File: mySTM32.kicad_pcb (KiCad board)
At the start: 2 copper layers, 138 x 108 mm, 122 parts, among them J1 conn1X2, J10 DB9_Female****, J11 USB_OTG, J12 conn2X16, J13 conn2X3, J14 Conn_02x02, J15 conn2X3, J16 conn1X2, J17 conn2X2, J18 JTAG, J19 Conn_02x17_Odd_Even, J2 USB_OTG, J20 Conn_02x22_Odd_Even, J21 conn2X9, J22 conn2X3, J23 Conn2x4, J3 conn2X3, J4 conn2X2, J5 conn2X2, J6 conn1X2, J7 Conn_01x02, J8 Conn2x4, J9 conn2X4, Q1 Q_NPN_BEC(S8050), Q2 Q_NPN_BEC, Q3 Q_NPN_BEC(S8050), SW1 KFT8.0, SW2 WAKUP, SW3 RESET, SW4 KE1, SW5 KEY2, U1 AT24C02, U2 W25Q16, U3 SD-Card, U4 SP3485, U5 SN65HVD230, U6 CH340G, U7 AMS1117, U8 SP3232, U9 STM32F103VET6, Y1 12MHz, Y2 32.768KHz, Y3 8MHz

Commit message: [IR Tx] [IR Rx]
Signed-off-by: EasonLiang <liangyx25@163.com>
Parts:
- moved R4 0.58 mm to (48.9, 117.2)
- moved R2 0.40 mm to (46.0, 117.1)
- moved R1 0.31 mm to (42.6, 117.1)
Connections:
- J5 pad 1: /IE -> /IR
- J5 pad 2: /PB1 -> /PB0
- J5 pad 3: /IR -> /IE
- J5 pad 4: /PB0 -> /PB1
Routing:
- net +3V3: track 140.4 -> 167.4 mm
- net /PB1: track 31.7 -> 53.5 mm
- net /PB0: track 34.0 -> 55.8 mm
- net Net-(D1-Pad1): track 0.00 -> 11.3 mm
- net Net-(D1-Pad2): track 0.00 -> 9.07 mm
- net /IR: track 0.00 -> 9.05 mm
- net Net-(Q1-Pad1): track 0.00 -> 8.27 mm
- net /IE: track 0.00 -> 8.22 mm
- net GND: track 89.5 -> 92.9 mm
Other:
- board text added: "PB0"
- board text added: "PB1"
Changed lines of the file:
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@@
   (general
     (thickness 1.6)
-    (drawings 99)
-    (tracks 556)
+    (drawings 101)
+    (tracks 587)
     (zones 0)
     (modules 122)
@@
   )
   (module Resistor_SMD:R_0805_2012Metric (layer F.Cu)
-    (at 48.91532 116.62156 270)
+    (at 48.87214 117.19814 270)
     (descr "Resistor SMD 0805 (2012 Metric), square (rectangular) end terminal, IPC_7351 nominal, (Body size source: IPC-SM-782 page 72, https://www.pcb-3d.com/wordpress/wp-content/uploads/ipc-sm-782a_amendment_1_and_2.pdf), generated with kicad-footprint-generator")
     (tags resistor)
@@
   )
   (module Resistor_SMD:R_0603_1608Metric (layer F.Cu)
-    (at 45.74032 116.82156 270)
+    (at 45.99686 117.12448 270)
     (descr "Resistor SMD 0603 (1608 Metric), square (rectangular) end terminal, IPC_7351 nominal, (Body size source: IPC-SM-782 page 72, https://www.pcb-3d.com/wordpress/wp-content/uploads/ipc-sm-782a_amendment_1_and_2.pdf), generated with kicad-footprint-generator")
     (tags resistor)
@@
   )
   (module Resistor_SMD:R_0603_1608Metric (layer F.Cu)
-    (at 42.56532 116.82156 90)
+    (at 42.57548 117.13464 90)
     (descr "Resistor SMD 0603 (1608 Metric), square (rectangular) end terminal, IPC_7351 nominal, (Body size source: IPC-SM-782 page 72, https://www.pcb-3d.com/wordpress/wp-content/uploads/ipc-sm-782a_amendment_1_and_2.pdf), generated with kicad-footprint-generator")
     (tags resistor)
@@
     (fp_line (start -1.27 2.54) (end 3.81 2.54) (layer F.SilkS) (width 0.12))
     (pad 4 thru_hole circle (at 2.54 -1.27) (size 1.6 1.6) (drill 1.02) (layers *.Cu *.Mask)
-      (net 45 /PB0))
+      (net 46 /PB1))
     (pad 3 thru_hole circle (at 2.54 1.27) (size 1.6 1.6) (drill 1.02) (layers *.Cu *.Mask)
-      (net 22 /IR))
+      (net 47 /IE))
     (pad 2 thru_hole circle (at 0 -1.27) (size 1.6 1.6) (drill 1.02) (layers *.Cu *.Mask)
-      (net 46 /PB1))
+      (net 45 /PB0))
     (pad 1 thru_hole rect (at 0 1.27) (size 1.6 1.6) (drill 1.02) (layers *.Cu *.Mask)
-      (net 47 /IE))
+      (net 22 /IR))
     (model ${KISYS3DMOD}/Connector_PinHeader_2.54mm.3dshapes/PinHeader_2x02_P2.54mm_Vertical.wrl
       (offset (xyz 0 -1 0))
@@
     )
   )
+  (gr_text PB1 (at 45.76064 104.3813) (layer F.SilkS)
+    (effects (font (size 1.2 1) (thickness 0.25)))
+  )
+  (gr_text PB0 (at 42.61612 104.3813) (layer F.SilkS)
+    (effects (font (size 1.2 1) (thickness 0.25)))
+  )
   (gr_text PB10 (at 137.09142 118.22938) (layer F.SilkS)
     (effects (font (size 1.2 1) (thickness 0.25)))
@@
   (gr_line (start 50.6984 121.8) (end 61.849 121.8) (layer F.SilkS) (width 0.12))
   (gr_line (start 50.6984 114.6) (end 50.6984 138) (layer F.SilkS) (width 0.12))
-  (gr_line (start 58.65368 103.67766) (end 30.05328 103.67766) (layer F.SilkS) (width 0.12))
+  (gr_line (start 58.65368 103.4) (end 30.05328 103.4) (layer F.SilkS) (width 0.12))
   (gr_line (start 58.6994 121.8) (end 58.6994 72.009) (layer F.SilkS) (width 0.12))
   (gr_line (start 30.0482 88.19526) (end 58.6994 88.19526) (layer F.SilkS) (width 0.12))
@@
   (segment (start 152.94386 114.81136) (end 152.94386 111.93018) (width 0.254) (layer F.Cu) (net 1))
   (segment (start 159.5755 121.443) (end 152.94386 114.81136) (width 0.254) (layer F.Cu) (net 1))
+  (segment (start 38.49878 115.4041) (end 37.85032 116.05256) (width 0.508) (layer F.Cu) (net 1))
+  (segment (start 38.49878 112.91346) (end 38.49878 115.4041) (width 0.508) (layer F.Cu) (net 1))
   (segment (start 96.880062 90.385849) (end 96.847552 90.385849) (width 0.254) (layer F.Cu) (net 3))
   (segment (start 92.443 85.916275) (end 92.443 85.344) (width 0.254) (layer F.Cu) (net 3))
@@
   (segment (start 140.87632 120.0785) (end 140.6652 120.28962) (width 0.254) (layer F.Cu) (net 3))
   (segment (start 143.3325 120.0785) (end 140.87632 120.0785) (width 0.254) (layer F.Cu) (net 3))
+  (segment (start 50.02615 129.55355) (end 54.5465 134.0739) (width 0.508) (layer F.Cu) (net 3))
+  (segment (start 50.02615 117.43965) (end 50.02615 129.55355) (width 0.508) (layer F.Cu) (net 3))
+  (segment (start 48.87214 116.28564) (end 50.02615 117.43965) (width 0.508) (layer F.Cu) (net 3))
+  (segment (start 38.49848 111.36376) (end 38.49878 111.36346) (width 0.508) (layer F.Cu) (net 3))
+  (segment (start 35.01898 111.36376) (end 38.49848 111.36376) (width 0.508) (layer F.Cu) (net 3))
+  (segment (start 38.49878 107.94696) (end 38.49878 108.0389) (width 0.508) (layer F.Cu) (net 3))
+  (segment (start 38.49878 108.0389) (end 38.49878 111.36346) (width 0.508) (layer F.Cu) (net 3))
   (segment (start 153.4795 74.4985) (end 153.29438 74.68362) (width 0.254) (layer F.Cu) (net 4))
   (segment (start 153.4795 71.361) (end 153.4795 74.4985) (width 0.254) (layer F.Cu) (net 4))
@@
   (segment (start 90.217394 85.81199) (end 88.36901 85.81199) (width 0.254) (layer F.Cu) (net 19))
   (segment (start 87.567 86.614) (end 83.833 86.614) (width 0.254) (layer F.Cu) (net 19))
+  (segment (start 48.87214 120.52554) (end 44.16552 125.23216) (width 0.508) (layer F.Cu) (net 20))
+  (segment (start 48.87214 118.11064) (end 48.87214 120.52554) (width 0.508) (layer F.Cu) (net 20))
+  (segment (start 35.85032 117.00256) (end 35.85032 116.91798) (width 0.254) (layer F.Cu) (net 21))
+  (segment (start 40.63192 122.69216) (end 44.16552 122.69216) (width 0.508) (layer F.Cu) (net 21))
+  (segment (start 35.85032 117.91056) (end 40.63192 122.69216) (width 0.508) (layer F.Cu) (net 21))
+  (segment (start 35.85032 117.00256) (end 35.85032 117.91056) (width 0.508) (layer F.Cu) (net 21))
+  (segment (start 35.01898 106.28376) (end 35.01898 106.4514) (width 0.508) (layer F.Cu) (net 22))
+  (segment (start 35.01898 106.4514) (end 38.34434 106.4514) (width 0.508) (layer F.Cu) (net 22))
+  (segment (start 38.49878 106.29696) (end 38.34434 106.4514) (width 0.508) (layer F.Cu) (net 22))
+  (segment (start 39.70578 106.29696) (end 42.62628 109.21746) (width 0.508) (layer F.Cu) (net 22))
+  (segment (start 38.49878 106.29696) (end 39.70578 106.29696) (width 0.508) (layer F.Cu) (net 22))
   (segment (start 151.7165 60.706) (end 151.78 60.6425) (width 0.508) (layer F.Cu) (net 23))
   (segment (start 149.034 60.706) (end 151.7165 60.706) (width 0.508) (layer F.Cu) (net 23))
@@
   (segment (start 90.48568 105.512999) (end 64.627001 105.512999) (width 0.254) (layer F.Cu) (net 45))
   (segment (start 95.112295 100.886384) (end 90.48568 105.512999) (width 0.254) (layer F.Cu) (net 45))
+  (segment (start 62.410459 105.550459) (end 63.5 106.64) (width 0.254) (layer F.Cu) (net 45))
+  (segment (start 43.753281 105.550459) (end 62.410459 105.550459) (width 0.254) (layer F.Cu) (net 45))
+  (segment (start 42.62628 106.67746) (end 43.753281 105.550459) (width 0.254) (layer F.Cu) (net 45))
   (segment (start 90.065787 106.64) (end 66.04 106.64) (width 0.254) (layer F.Cu) (net 46))
   (segment (start 95.465849 101.239938) (end 90.065787 106.64) (width 0.254) (layer F.Cu) (net 46))
+  (segment (start 65.167962 106.64) (end 66.04 106.64) (width 0.254) (layer F.Cu) (net 46))
+  (segment (start 64.040961 107.767001) (end 65.167962 106.64) (width 0.254) (layer F.Cu) (net 46))
+  (segment (start 46.255821 107.767001) (end 64.040961 107.767001) (width 0.254) (layer F.Cu) (net 46))
+  (segment (start 45.16628 106.67746) (end 46.255821 107.767001) (width 0.254) (layer F.Cu) (net 46))
+  (segment (start 45.16628 109.21746) (end 45.16628 113.81486) (width 0.508) (layer F.Cu) (net 47))
+  (segment (start 42.6715 116.30964) (end 42.57548 116.30964) (width 0.508) (layer F.Cu) (net 47))
+  (segment (start 45.16628 113.81486) (end 42.6715 116.30964) (width 0.508) (layer F.Cu) (net 47))
   (segment (start 136.1148 36.53612) (end 132.98882 39.6621) (width 0.254) (layer F.Cu) (net 48))
   (segment (start 136.1148 34.1122) (end 136.1148 36.53612) (width 0.254) (layer F.Cu) (net 48))
@@
   (segment (start 126.463145 66) (end 129.54 66) (width 0.254) (layer F.Cu) (net 149))
   (segment (start 104.198617 88.264528) (end 126.463145 66) (width 0.254) (layer F.Cu) (net 149))
+  (segment (start 37.85032 117.95256) (end 46.12136 117.95256) (width 0.508) (layer F.Cu) (net 153))
   (segment (start 143.02058 63.49492) (end 142.9995 63.516) (width 0.254) (layer F.Cu) (net 154))
   (segment (start 146.73884 63.49492) (end 143.02058 63.49492) (width 0.254) (layer F.Cu) (net 154))

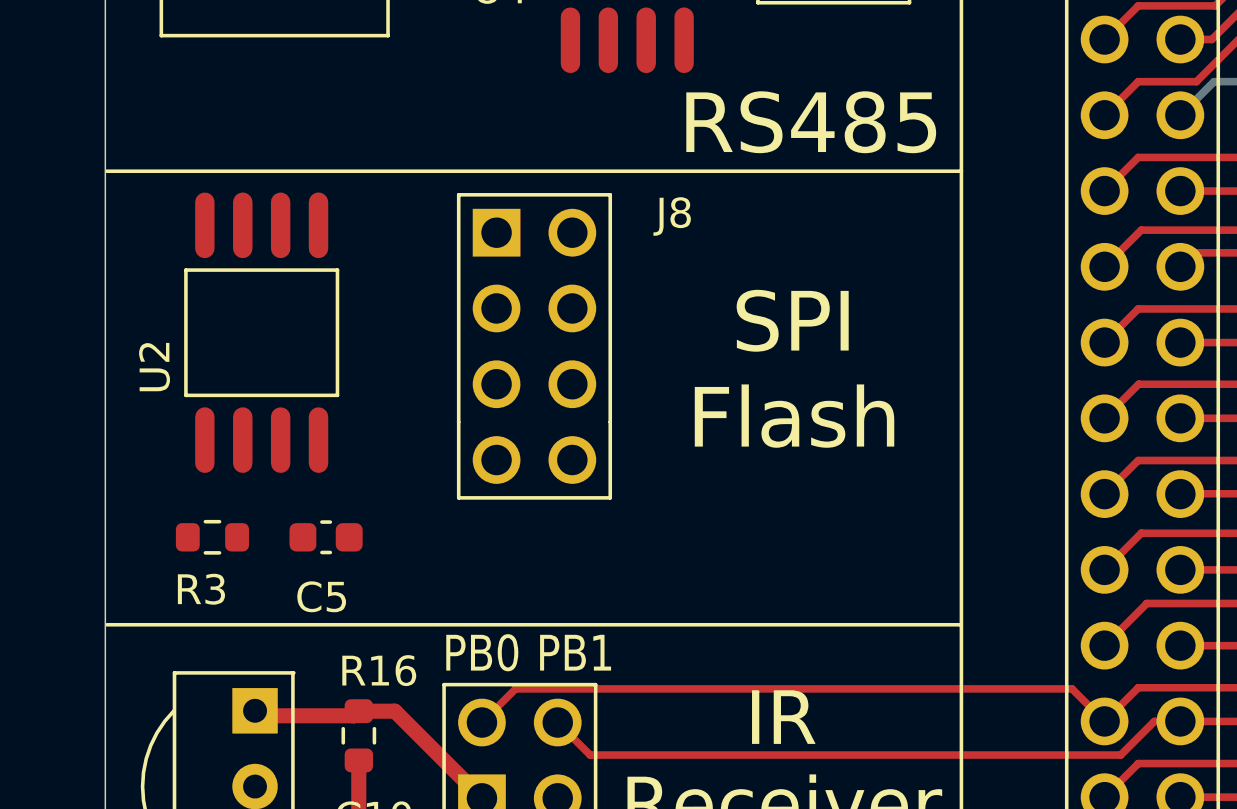
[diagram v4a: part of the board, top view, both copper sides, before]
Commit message: [SPI Flash]
Signed-off-by: EasonLiang <liangyx25@163.com>
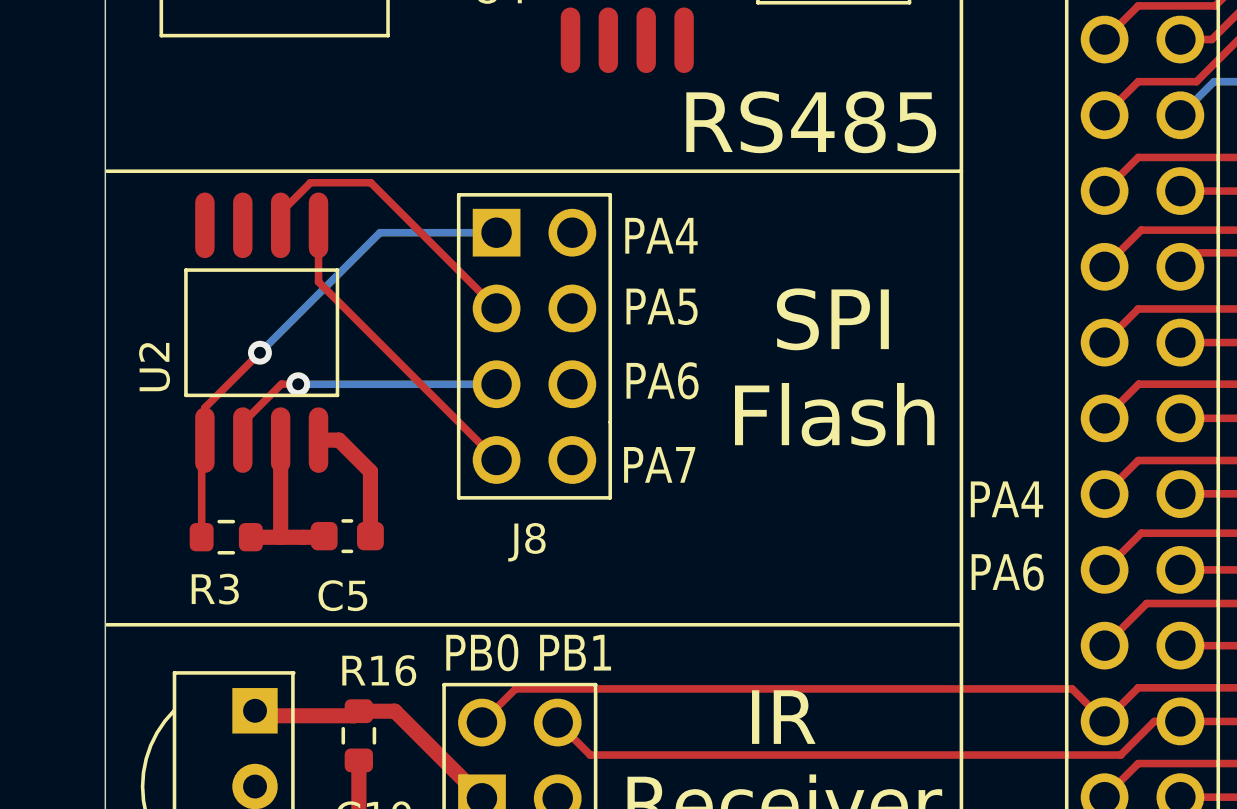
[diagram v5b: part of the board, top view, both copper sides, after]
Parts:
- moved C5 0.71 mm to (38.1, 100.4)
- moved R3 0.46 mm to (34.1, 100.5)
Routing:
- net /FLASH_CS: track 0.00 -> 16.6 mm, vias 0 -> 1
- net /FLASH_MOSI: track 0.00 -> 10.3 mm
- net /FLASH_CLK: track 0.00 -> 9.83 mm
- net /FLASH_MISO: track 0.00 -> 9.62 mm, vias 0 -> 1
- net +3V3: track 167.4 -> 173.5 mm
- net GND: track 92.9 -> 97.3 mm
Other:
- board text added: "PA4"
- board text added: "PA5"
- board text added: "PA6"
- board text added: "PA7"

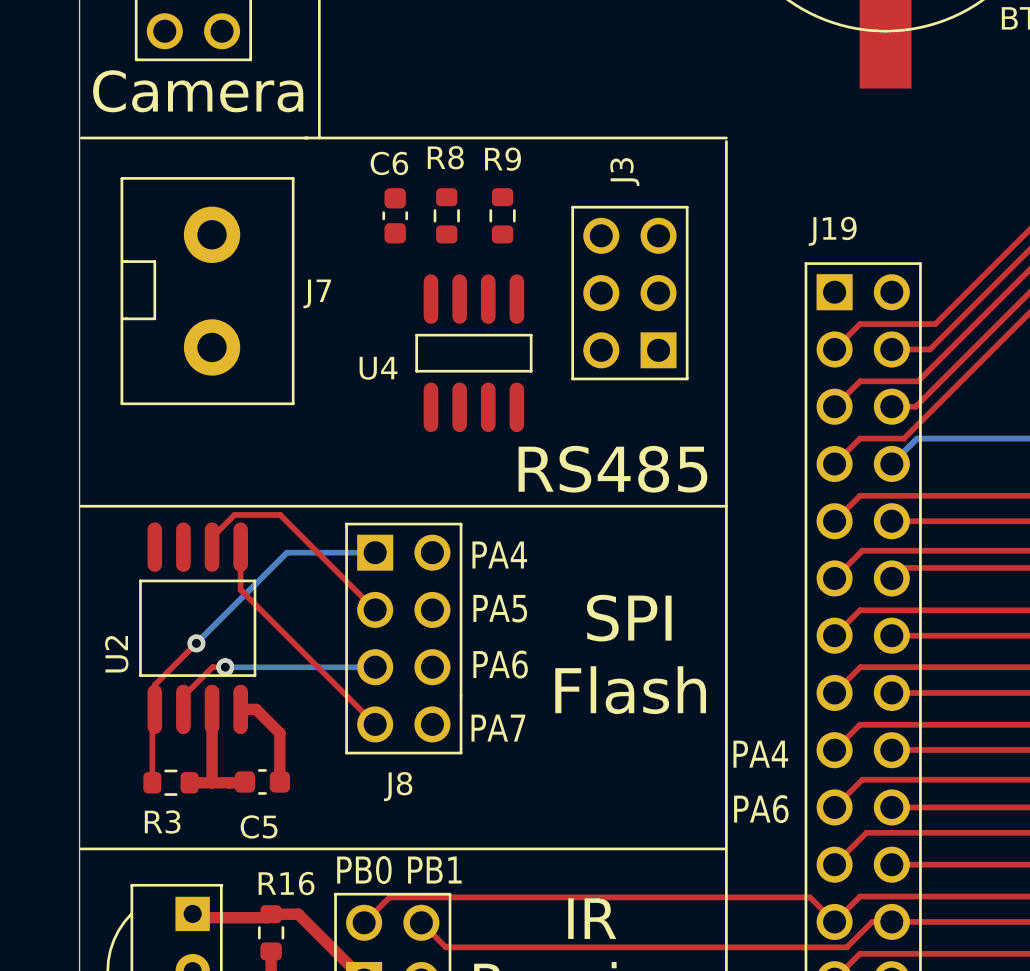
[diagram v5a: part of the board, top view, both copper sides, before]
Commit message: [RS485]
Signed-off-by: EasonLiang <liangyx25@163.com>
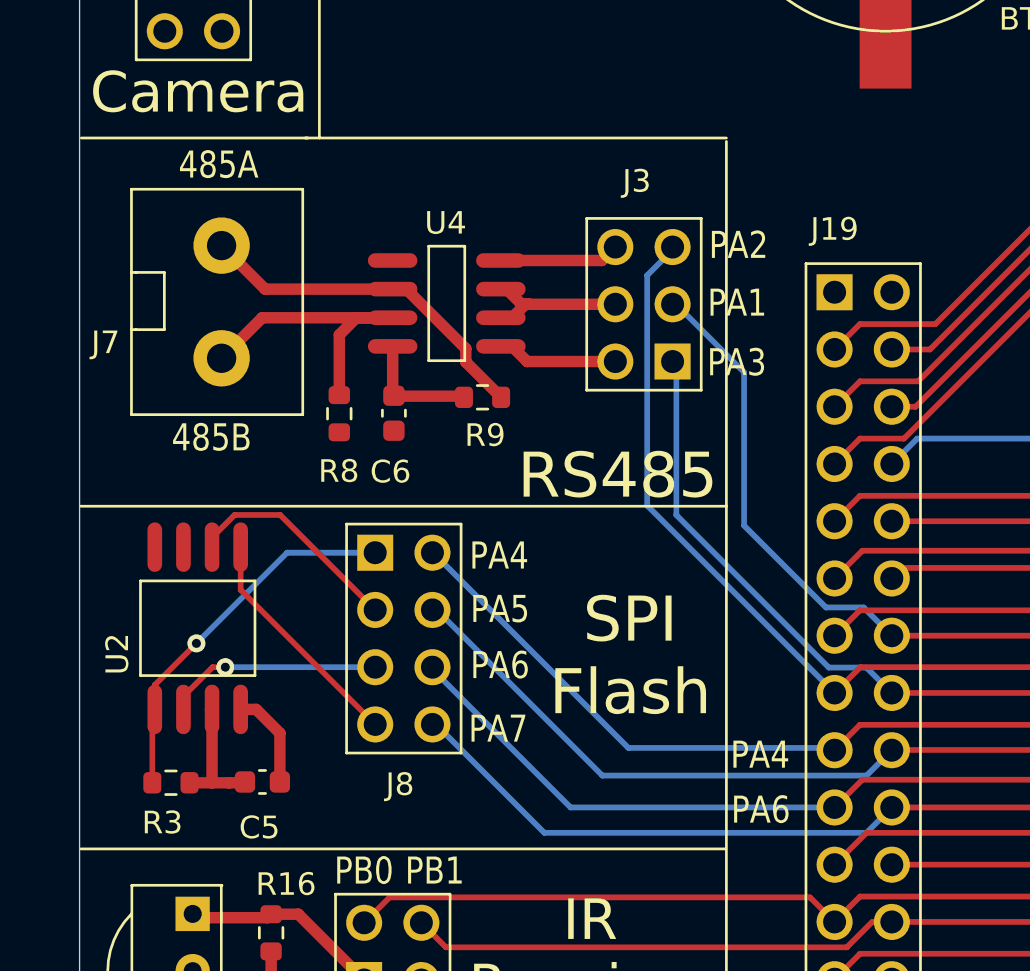
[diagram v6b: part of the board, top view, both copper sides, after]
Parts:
- moved R8 9.99 mm to (41.5, 84.1), turned to 270 degrees
- moved C6 8.76 mm to (43.9, 84.1), turned to 90 degrees
- moved R9 8.10 mm to (47.9, 83.4), turned to 180 degrees
- moved U4 2.52 mm to (46.3, 79.2), turned to 90 degrees
- moved J3 0.80 mm to (55.0, 81.8)
- moved J7 0.64 mm to (36.3, 81.6)
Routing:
- net /PA5: track 28.2 -> 52.1 mm
- net /PA2: track 28.9 -> 52.6 mm
- net /PA7: track 28.7 -> 51.6 mm
- net /PA4: track 30.8 -> 52.3 mm
- net /PA6: track 31.3 -> 51.8 mm
- net /PA1: track 27.3 -> 47.3 mm
- net /PA3: track 26.4 -> 46.2 mm
- net Net-(J7-Pad2): track 0.00 -> 15.5 mm
- net Net-(J7-Pad1): track 0.00 -> 15.0 mm
- net Net-(J3-Pad4): track 0.00 -> 7.05 mm
- net +3V3: track 173.5 -> 178.9 mm
- net Net-(J3-Pad2): track 0.00 -> 5.36 mm
- net Net-(J3-Pad6): track 0.00 -> 5.33 mm
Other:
- board text added: "485A"
- board text added: "485B"
- board text added: "PA1"
- board text added: "PA2"
- board text added: "PA3"

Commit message: [JTAG]
Signed-off-by: EasonLiang <liangyx25@163.com>
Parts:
- moved C19 10.5 mm to (149.4, 125.4), turned to 0 degrees
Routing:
- net /NJTRST: track 33.8 -> 105.4 mm
- net /JTDI: track 21.2 -> 76.9 mm, vias 0 -> 1
- net /JTDO: track 30.0 -> 84.3 mm, vias 0 -> 1
- net /JTCK_SWCLK: track 23.5 -> 77.0 mm, vias 0 -> 1
- net /JTMS_SWDIO: track 22.9 -> 74.9 mm, vias 0 -> 1
- net GND: track 97.3 -> 118.0 mm
- net +3V3: track 178.9 -> 194.6 mm
